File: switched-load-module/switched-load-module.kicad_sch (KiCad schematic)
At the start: 3 parts

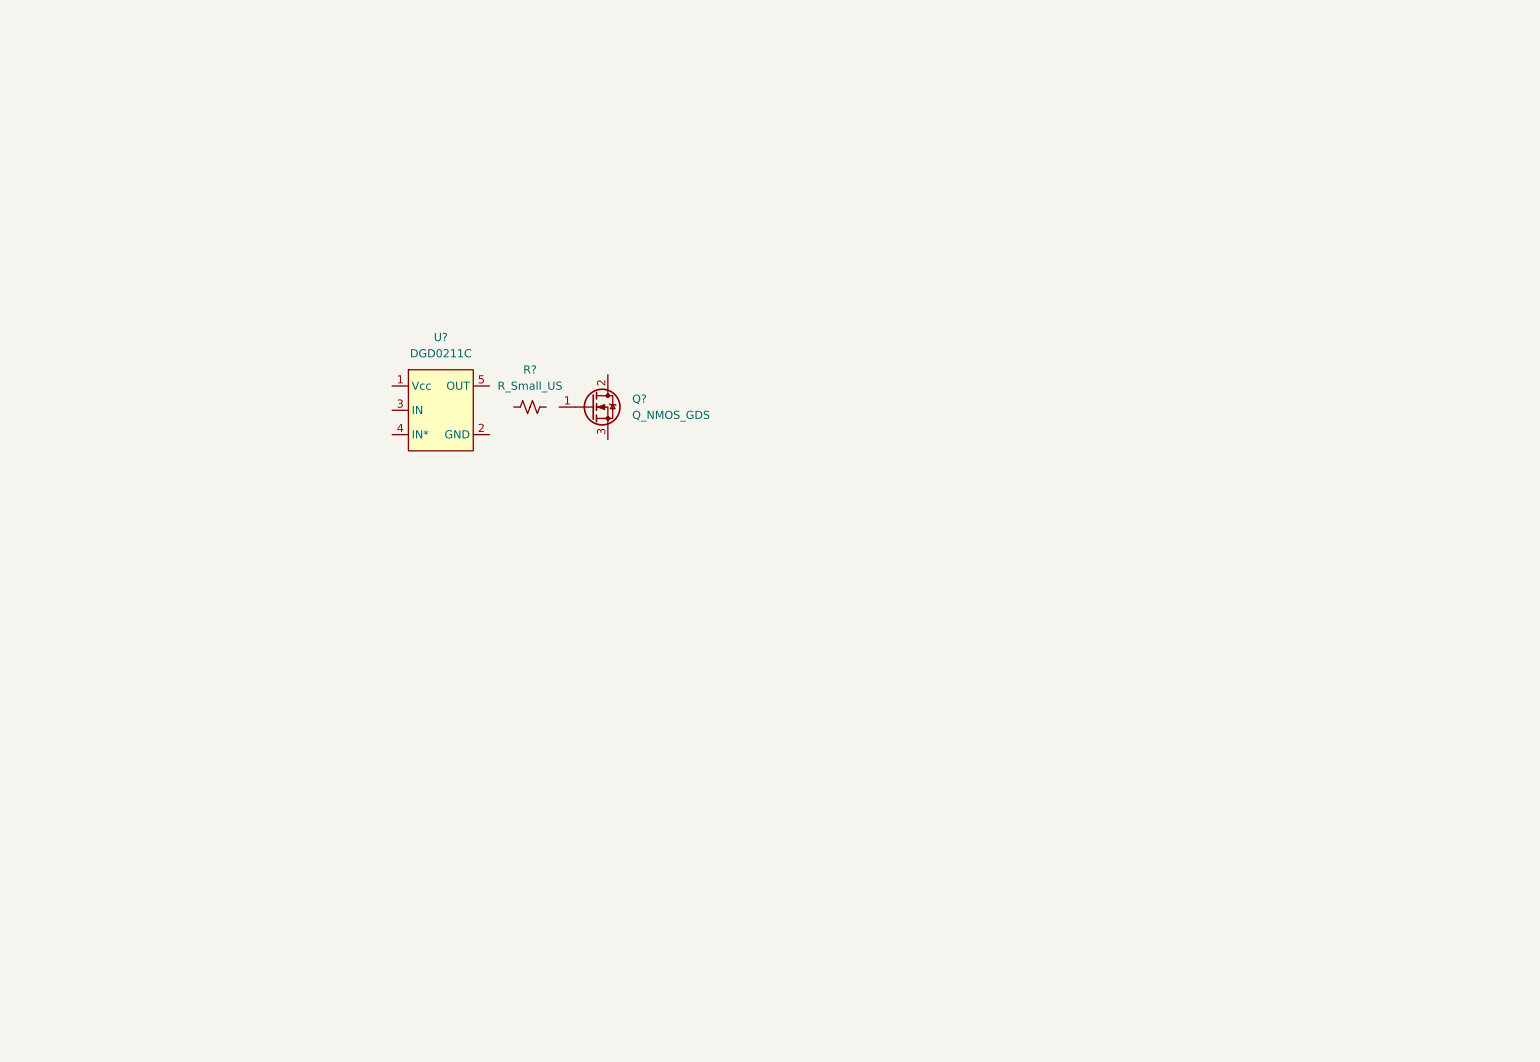
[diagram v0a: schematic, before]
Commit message: Finishing switched load module
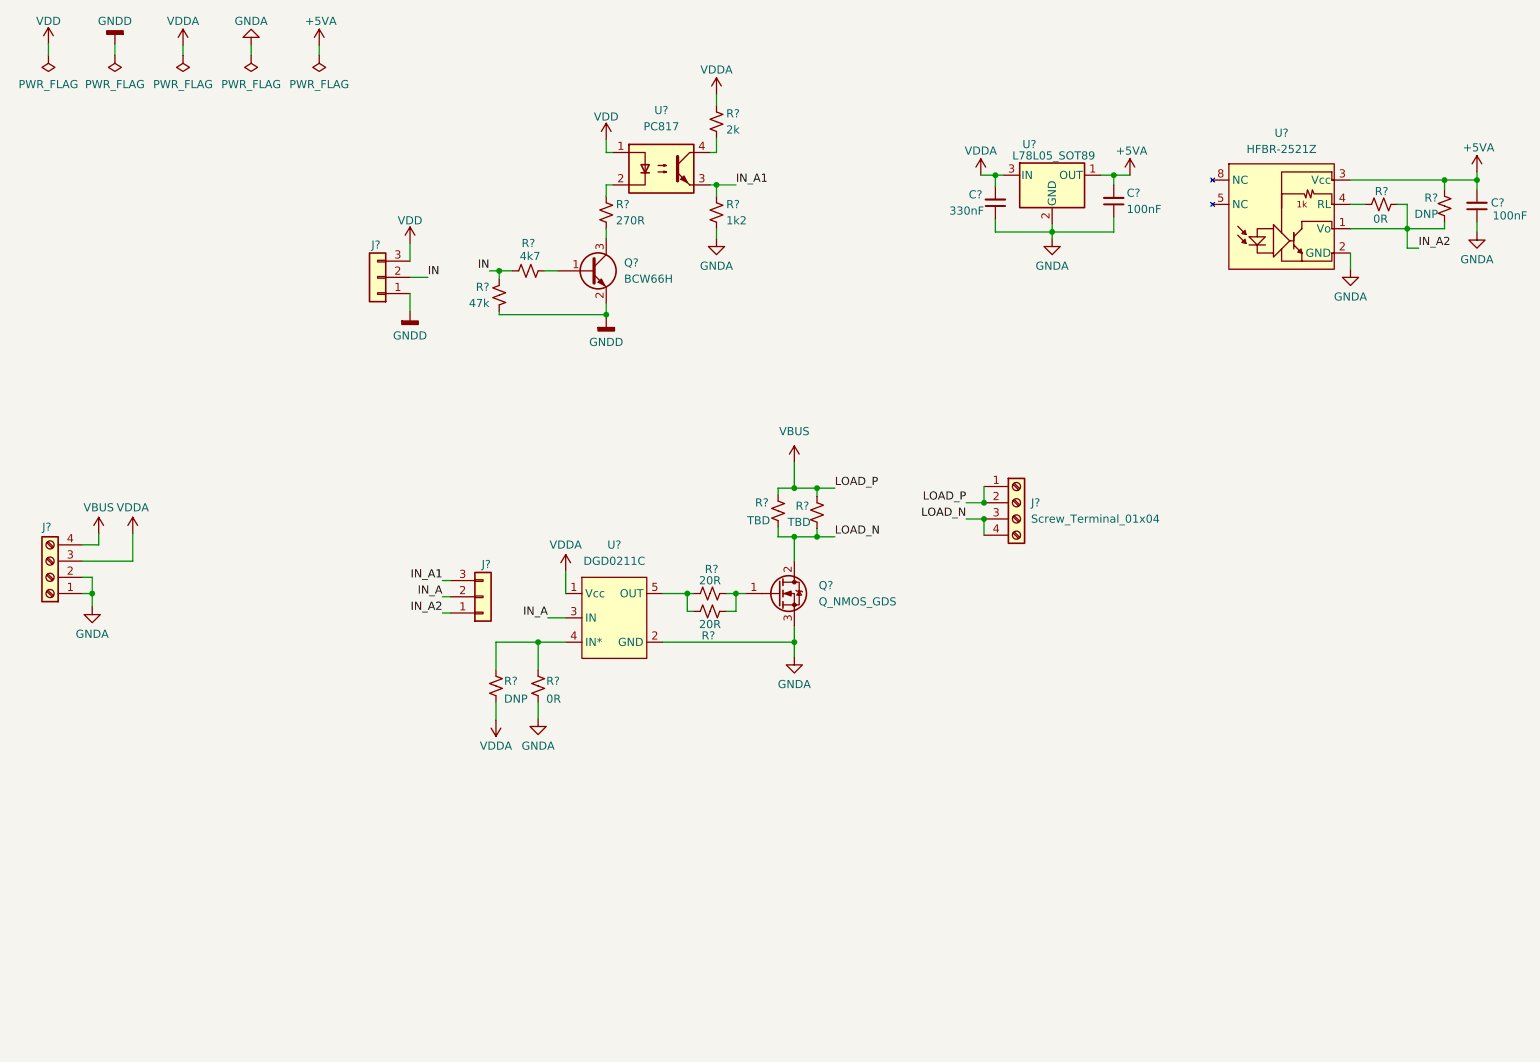
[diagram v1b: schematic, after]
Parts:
- added C?: 330nF, Capacitor_SMD:C_0805_2012Metric_Pad1.18x1.45mm_HandSolder, symbol Device:C_Small
- added C? (x2): 100nF, Capacitor_SMD:C_0805_2012Metric_Pad1.18x1.45mm_HandSolder, symbol Device:C_Small
- added J? (x2): Screw_Terminal_01x04, TerminalBlock_Phoenix:TerminalBlock_Phoenix_MKDS-1,5-4-5.08_1x04_P5.08mm_Horizontal, symbol Connector:Screw_Terminal_01x04
- added J? (x2): Conn_01x03, Connector_PinHeader_2.54mm:PinHeader_1x03_P2.54mm_Vertical, symbol Connector_Generic:Conn_01x03
- added Q?: BCW66H, Package_TO_SOT_SMD:SOT-23W, symbol Device:Q_NPN_BEC
- added R?: 2k, Resistor_SMD:R_0805_2012Metric_Pad1.20x1.40mm_HandSolder, symbol Device:R_Small_US
- added R? (x2): DNP, Resistor_SMD:R_0805_2012Metric_Pad1.20x1.40mm_HandSolder, symbol Device:R_Small_US
- added R? (x2): 0R, Resistor_SMD:R_0805_2012Metric_Pad1.20x1.40mm_HandSolder, symbol Device:R_Small_US
- added R?: 20R, Resistor_SMD:R_MELF_MMB-0207, symbol Device:R_Small_US
- added R? (x2): TBD, Resistor_THT:R_Axial_Power_L60.0mm_W14.0mm_P71.12mm, symbol Device:R_Small_US
- added R?: 270R, Resistor_SMD:R_0805_2012Metric_Pad1.20x1.40mm_HandSolder, symbol Device:R_Small_US
- added R?: 1k2, Resistor_SMD:R_0805_2012Metric_Pad1.20x1.40mm_HandSolder, symbol Device:R_Small_US
- added R?: 4k7, Resistor_SMD:R_0805_2012Metric_Pad1.20x1.40mm_HandSolder, symbol Device:R_Small_US
- added R?: 47k, Resistor_SMD:R_0805_2012Metric_Pad1.20x1.40mm_HandSolder, symbol Device:R_Small_US
- added U?: HFBR-2521Z, symbol CL_Fiber_Optic:HFBR-2521Z
- added U?: PC817, Package_DIP:DIP-4_W8.89mm_SMDSocket_LongPads, symbol Isolator:PC817
- added U?: L78L05_SOT89, Package_TO_SOT_SMD:SOT-89-3, symbol Regulator_Linear:L78L05_SOT89
- R?: value R_Small_US -> 20R; footprint (none) -> Resistor_SMD:R_MELF_MMB-0207
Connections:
- net at Q?.1 (G): now also R?.2, R?.1
- net LOAD_N: now reaches Q?.2 (D)
- net LOAD_N: now also J?.3 (Pin_3), J?.4 (Pin_4), R?.1, R?.1
- net GNDA: now reaches Q?.3 (S)
- net GNDA: now also U?.2 (GND), C?.1, C?.1, C?.1, J?.1 (Pin_1), J?.2 (Pin_2), R?.2, R?.2, U?.2 (GND), U?.2 (GND)
- net at R?.1: now also U?.5 (OUT), R?.2
- net VDDA: now reaches U?.1 (Vcc)
- net VDDA: now also C?.2, J?.3 (Pin_3), R?.1, R?.2, U?.3 (IN)
- net IN_A: now reaches U?.3 (IN)
- net IN_A: now also J?.2 (Pin_2)
- net at U?.4 (IN*): now also R?.1, R?.1
- new net: R?.2, U?.4
- new net: R?.2, U?.4 (RL)
- new net: R?.1, U?.2
- new net: Q?.3 (C), R?.2
- new net: Q?.1 (B), R?.2
- new net +5VA: C?.2, C?.2, R?.2, U?.1 (OUT), U?.3 (Vcc)
- new net GNDD: J?.1 (Pin_1), Q?.2 (E), R?.1
- new net IN: J?.2 (Pin_2), R?.1, R?.2
- new net IN_A1: J?.3 (Pin_3), R?.1, U?.3
- new net IN_A2: J?.1 (Pin_1), R?.1, R?.1, U?.1 (Vo)
- new net VBUS: J?.1 (Pin_1), J?.2 (Pin_2), J?.4 (Pin_4), R?.2, R?.2
- new net VDD: J?.3 (Pin_3), U?.1
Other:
- moved on the sheet: Q?, R?, U?

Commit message: Added switched load board
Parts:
- removed J?: Screw_Terminal_01x04, TerminalBlock_Phoenix:TerminalBlock_Phoenix_MKDS-1,5-4-5.08_1x04_P5.08mm_Horizontal, symbol Connector:Screw_Terminal_01x04
- added C4, C5: 10uF, Capacitor_SMD:C_0805_2012Metric_Pad1.18x1.45mm_HandSolder, symbol Device:C_Small
- added C6: 100nF, Capacitor_SMD:C_0805_2012Metric_Pad1.18x1.45mm_HandSolder, symbol Device:C_Small
- added D1: LED, LED_SMD:LED_0805_2012Metric_Pad1.15x1.40mm_HandSolder, symbol Device:LED
- added J4: Screw_Terminal_01x05, TerminalBlock_Phoenix:TerminalBlock_Phoenix_MKDS-1,5-5-5.08_1x05_P5.08mm_Horizontal, symbol Connector:Screw_Terminal_01x05
- added R14: 1k2, Resistor_SMD:R_0805_2012Metric_Pad1.20x1.40mm_HandSolder, symbol Device:R_Small_US
- R8, R9: renamed from R?; footprint Resistor_THT:R_Axial_Power_L60.0mm_W14.0mm_P71.12mm -> Resistor_THT:R_Axial_Power_L38.0mm_W9.0mm_P45.72mm
- U3: renamed from U?; footprint (none) -> CL_Fiber_Optic:HFBR-2521Z
- gave numbers to parts that had none: 22
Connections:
- net GNDA: now also C4.1, C5.1, C6.1, J4.1 (Pin_1), J4.2 (Pin_2), R14.2
- net LOAD_N: now also J2.1 (Pin_1), J2.2 (Pin_2); no longer J2.3 (Pin_3), J2.4 (Pin_4)
- net VBUS: now also J2.3 (Pin_3), J2.4 (Pin_4), J4.3 (Pin_3), J4.4 (Pin_4); no longer J2.1 (Pin_1), J2.2 (Pin_2)
- net VDDA: now also C4.2, C5.2, C6.2, J4.5 (Pin_5)
- net at R10.1, R11.2, U4.5 (OUT): now also D1.2 (A)
- new net: D1.1 (K), R14.1
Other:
- moved on the sheet: C1, C2, C3, J1, J2, J3, Q1, Q2, R1, R10, R11, R12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

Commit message: Added diode for switched load module
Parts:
- added D2: D, Diode_SMD:D_SMA, symbol Device:D
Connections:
- net GNDA: now also D2.2 (A)
- net LOAD_N: now also D2.1 (K)
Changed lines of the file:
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@@
   (junction (at 36.322 163.322) (diameter 0) (color 0 0 0 0)
   )
+  (junction (at 134.366 152.4) (diameter 0) (color 0 0 0 0)
+  )
   (junction (at 83.82 166.624) (diameter 0) (color 0 0 0 0)
   )
+  (junction (at 134.366 166.116) (diameter 0) (color 0 0 0 0)
+  )
   (wire (pts (xy 106.68 109.982) (xy 106.68 111.252))
     (stroke (width 0) (type default) (color 0 0 0 0))
@@
     (stroke (width 0) (type default) (color 0 0 0 0))
   )
-  (wire (pts (xy 134.366 150.114) (xy 134.366 153.924))
+  (wire (pts (xy 134.366 150.114) (xy 134.366 152.4))
     (stroke (width 0) (type default) (color 0 0 0 0))
   )
@@
     (stroke (width 0) (type default) (color 0 0 0 0))
   )
+  (wire (pts (xy 134.366 166.116) (xy 134.366 168.91))
+    (stroke (width 0) (type default) (color 0 0 0 0))
+  )
   (wire (pts (xy 78.994 148.59) (xy 78.994 149.606))
     (stroke (width 0) (type default) (color 0 0 0 0))
@@
     (stroke (width 0) (type default) (color 0 0 0 0))
   )
+  (wire (pts (xy 134.366 152.4) (xy 134.366 153.924))
+    (stroke (width 0) (type default) (color 0 0 0 0))
+  )
   (wire (pts (xy 31.242 119.38) (xy 40.132 119.38))
     (stroke (width 0) (type default) (color 0 0 0 0))
   )
+  (wire (pts (xy 139.954 163.068) (xy 139.954 166.116))
+    (stroke (width 0) (type default) (color 0 0 0 0))
+  )
   (wire (pts (xy 69.596 155.956) (xy 69.596 157.226))
     (stroke (width 0) (type default) (color 0 0 0 0))
@@
     (stroke (width 0) (type default) (color 0 0 0 0))
   )
+  (wire (pts (xy 139.954 155.448) (xy 139.954 152.4))
+    (stroke (width 0) (type default) (color 0 0 0 0))
+  )
   (wire (pts (xy 111.252 159.004) (xy 111.252 162.56))
     (stroke (width 0) (type default) (color 0 0 0 0))
   )
-  (wire (pts (xy 134.366 164.084) (xy 134.366 168.91))
+  (wire (pts (xy 134.366 164.084) (xy 134.366 166.116))
+    (stroke (width 0) (type default) (color 0 0 0 0))
+  )
+  (wire (pts (xy 134.366 152.4) (xy 139.954 152.4))
+    (stroke (width 0) (type default) (color 0 0 0 0))
+  )
+  (wire (pts (xy 139.954 166.116) (xy 134.366 166.116))
     (stroke (width 0) (type default) (color 0 0 0 0))
   )
@@
   )
   (symbol (lib_id "Device:Q_NMOS_GDS") (at 131.826 159.004 0) (unit 1)
-    (in_bom yes) (on_board yes) (fields_autoplaced)
-    (property "Reference" "Q2" (id 0) (at 138.176 157.7339 0)
+    (in_bom yes) (on_board yes)
+    (property "Reference" "Q2" (id 0) (at 128.778 155.448 0)
       (effects (font (size 1.27 1.27)) (justify left))
     )
     (property "Value" "Q_NMOS_GDS" (id 1) (at 138.176 160.2739 0)
-      (effects (font (size 1.27 1.27)) (justify left))
+      (effects (font (size 1.27 1.27)) (justify left) hide)
     )
     (property "Footprint" "Package_TO_SOT_SMD:TO-252-2" (id 2) (at 136.906 156.464 0)
@@
     (pin "1")
   )
+  (symbol (lib_id "Device:D") (at 139.954 159.258 270) (unit 1)
+    (in_bom yes) (on_board yes) (fields_autoplaced)
+    (property "Reference" "D2" (id 0) (at 141.986 157.9879 90)
+      (effects (font (size 1.27 1.27)) (justify left))
+    )
+    (property "Value" "D" (id 1) (at 141.986 160.5279 90)
+      (effects (font (size 1.27 1.27)) (justify left))
+    )
+    (property "Footprint" "Diode_SMD:D_SMA" (id 2) (at 139.954 159.258 0)
+      (effects (font (size 1.27 1.27)) hide)
+    )
+    (property "Datasheet" "~" (id 3) (at 139.954 159.258 0)
+      (effects (font (size 1.27 1.27)) hide)
+    )
+    (pin "1")
+    (pin "2")
+  )
   (symbol (lib_id "Device:R_Small_US") (at 101.6 115.316 180) (unit 1)
     (in_bom yes) (on_board yes)
@@
       (reference "D1") (unit 1) (value "LED") (footprint "LED_SMD:LED_0805_2012Metric_Pad1.15x1.40mm_HandSolder")
     )
+    (path "/e4b6476f-dad2-4c67-87f6-bde3a7af52ab"
+      (reference "D2") (unit 1) (value "D") (footprint "Diode_SMD:D_SMA")
+    )
     (path "/a62ffd0a-3499-4c01-a3b9-f2f464fa9d52"

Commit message: Added LEDs to switched load module
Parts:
- added D3, D4: LED, LED_SMD:LED_0805_2012Metric_Pad1.15x1.40mm_HandSolder, symbol Device:LED
- added R15, R16: 2k, Resistor_SMD:R_0805_2012Metric_Pad1.20x1.40mm_HandSolder, symbol Device:R_Small_US
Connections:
- net GNDA: now also R16.1
- net GNDD: now also R15.1
- net VDD: now also D3.2 (A)
- net VDDA: now also D4.2 (A)
- new net: D4.1 (K), R16.2
- new net: D3.1 (K), R15.2
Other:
- moved on the sheet: J1, Q1, R1, R2, R3, R4, R5, U1
